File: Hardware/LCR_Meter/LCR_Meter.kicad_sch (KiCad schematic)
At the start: 0 parts

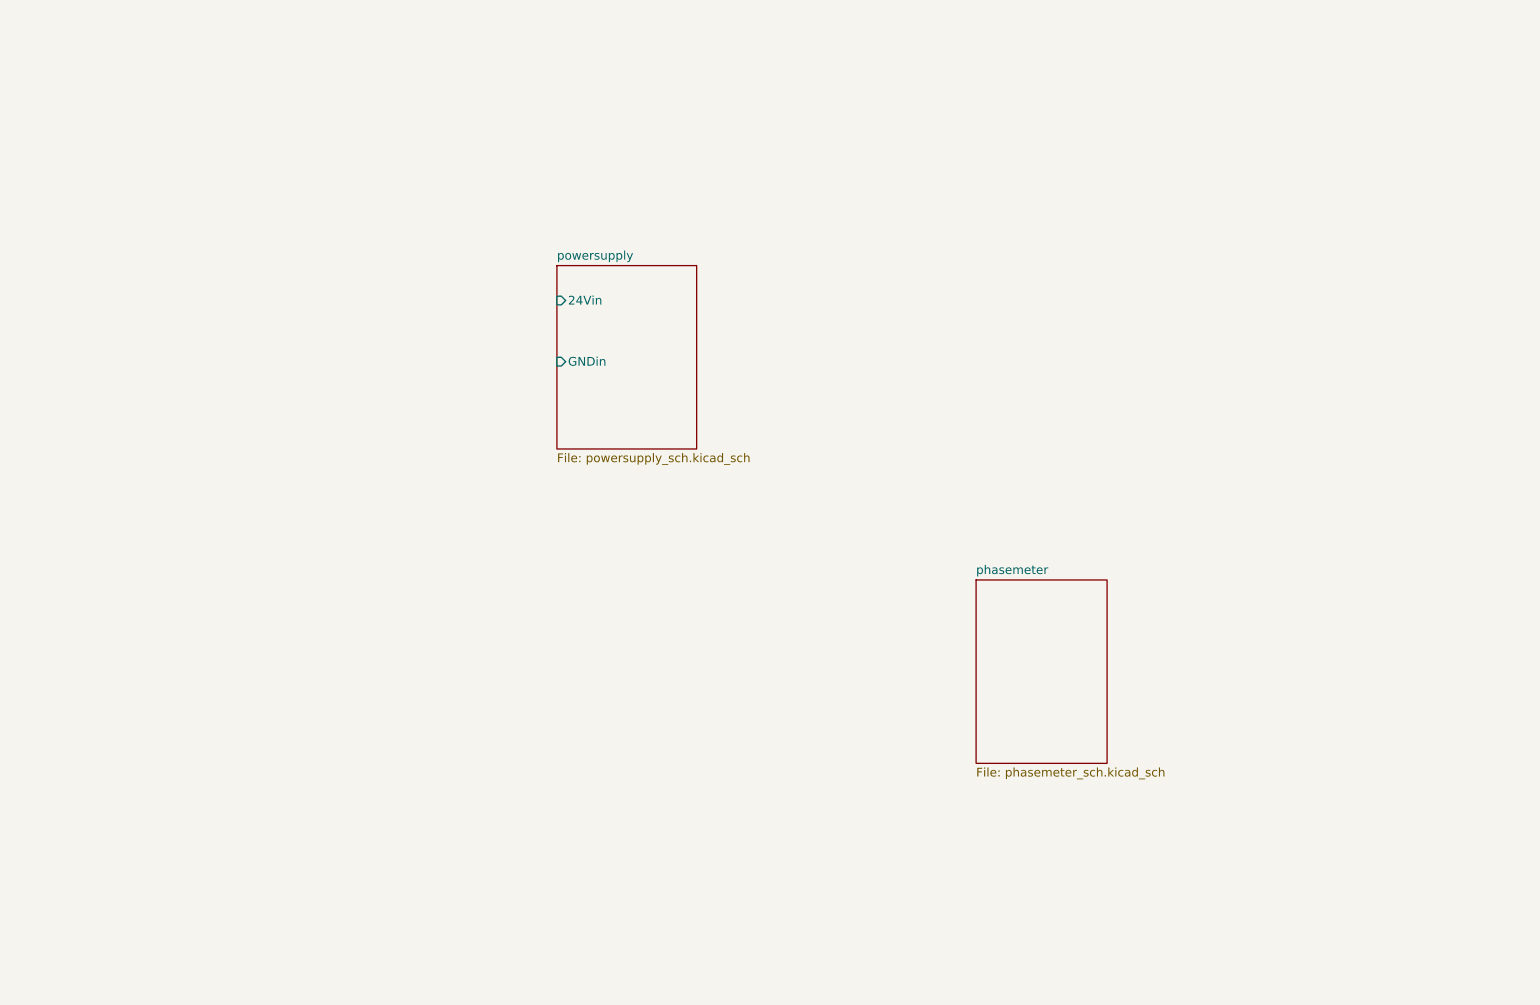
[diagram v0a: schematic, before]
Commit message: work on schematic block diagramm
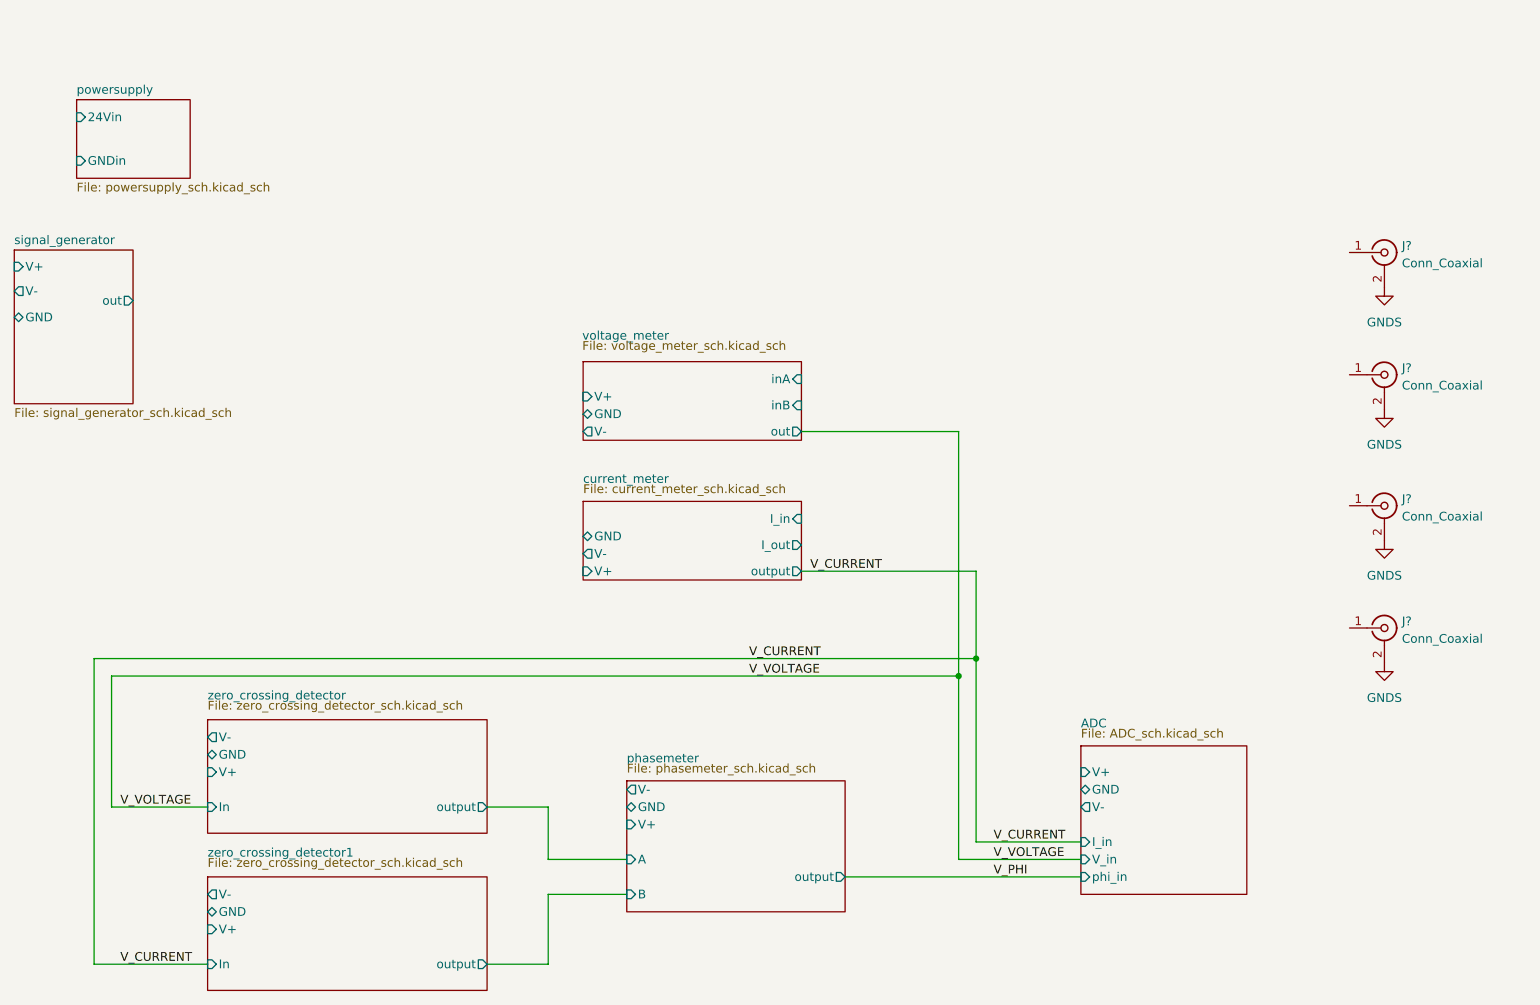
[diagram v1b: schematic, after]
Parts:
- added J? (x4): Conn_Coaxial, symbol Connector:Conn_Coaxial
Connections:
- new net GNDS: J?.2 (Ext), J?.2 (Ext), J?.2 (Ext), J?.2 (Ext)
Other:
- added sheet ADC (ADC_sch.kicad_sch)
- added sheet current_meter (current_meter_sch.kicad_sch)
- added sheet signal_generator (signal_generator_sch.kicad_sch)
- added sheet voltage_meter (voltage_meter_sch.kicad_sch)
- added sheet zero_crossing_detector (zero_crossing_detector_sch.kicad_sch)
- added sheet zero_crossing_detector1 (zero_crossing_detector_sch.kicad_sch)
- sheet phasemeter ports: added A, B, GND, V+, V-, output; removed none

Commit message: work on KCR schematic
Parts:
- J?: value Conn_Coaxial -> L_CUR; footprint (none) -> Connector_Coaxial:SMA_Amphenol_132291-12_Vertical
- J?: value Conn_Coaxial -> H_POT; footprint (none) -> Connector_Coaxial:SMA_Amphenol_132291-12_Vertical
- J?: value Conn_Coaxial -> L_POT; footprint (none) -> Connector_Coaxial:SMA_Amphenol_132291-12_Vertical
- J?: value Conn_Coaxial -> H_CUR; footprint (none) -> Connector_Coaxial:SMA_Amphenol_132291-12_Vertical
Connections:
- net L_CUR: now reaches J?.1 (In)
- net H_POT: now reaches J?.1 (In)
- net L_POT: now reaches J?.1 (In)
- net H_CUR: now reaches J?.1 (In)
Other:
- sheet phasemeter renamed zerocrossing_phase_detector
- removed sheet zero_crossing_detector
- removed sheet zero_crossing_detector1
- added sheet activ_rectifiers (activ_rectifiers_sch.kicad_sch)
- sheet current_meter ports: added none; removed I_out
- sheet zerocrossing_phase_detector: file phasemeter_sch.kicad_sch -> zerocrossing_phase_detector_sch.kicad_sch
- moved on the sheet: J?

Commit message: work on Phase detector
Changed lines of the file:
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@@
       (effects (font (size 1.27 1.27)) (justify right))
-    )
-    (pin "V-" output (at 120.65 127 180)
-      (effects (font (size 1.27 1.27)) (justify left))
     )
     (pin "GND" bidirectional (at 120.65 129.54 180)
@@
     )
     (pin "V+" input (at 120.65 132.08 180)
+      (effects (font (size 1.27 1.27)) (justify left))
+    )
+    (pin "V-" input (at 120.65 127 180)
       (effects (font (size 1.27 1.27)) (justify left))
     )
@@
       (reference "#PWR0104") (unit 1) (value "GNDS") (footprint "")
     )
+    (path "/d1422d36-ee99-4795-804f-b865553c7f13/08a9b504-957a-452e-9508-e5b0b1205a5d"
+      (reference "C?") (unit 1) (value "100n") (footprint "Capacitor_SMD:C_0805_2012Metric_Pad1.18x1.45mm_HandSolder")
+    )
     (path "/3366fbd2-b7c6-4ccb-afdd-03c00c73e9fc/098ad0ae-aeb1-42c0-bb17-5236427ef036"
       (reference "C?") (unit 1) (value "100n") (footprint "Capacitor_SMD:C_1206_3216Metric")
     )
+    (path "/d1422d36-ee99-4795-804f-b865553c7f13/0bd4f34c-719a-4a2f-9253-4be87b4fffea"
+      (reference "C?") (unit 1) (value "100n") (footprint "Capacitor_SMD:C_0805_2012Metric_Pad1.18x1.45mm_HandSolder")
+    )
     (path "/3366fbd2-b7c6-4ccb-afdd-03c00c73e9fc/3840940d-b0c9-4ab7-8bfa-8ee653f9a3e6"
       (reference "C?") (unit 1) (value "100n") (footprint "Capacitor_SMD:C_1206_3216Metric")
     )
+    (path "/d1422d36-ee99-4795-804f-b865553c7f13/ba98c343-27f7-433c-a31e-e5c72a4732e8"
+      (reference "C?") (unit 1) (value "100n") (footprint "Capacitor_SMD:C_0805_2012Metric_Pad1.18x1.45mm_HandSolder")
+    )
+    (path "/d1422d36-ee99-4795-804f-b865553c7f13/c7cb2033-4bc4-4f5b-9f35-08da814285af"
+      (reference "C?") (unit 1) (value "100n") (footprint "Capacitor_SMD:C_0805_2012Metric_Pad1.18x1.45mm_HandSolder")
+    )
     (path "/3366fbd2-b7c6-4ccb-afdd-03c00c73e9fc/0b3f0e18-090c-4545-bbd0-c5e5f41d899e"
       (reference "D?") (unit 1) (value "MMBD301LT3G") (footprint "Package_TO_SOT_SMD:SOT-23")
@@
       (reference "R?") (unit 1) (value "10k") (footprint "Resistor_SMD:R_1206_3216Metric")
     )
+    (path "/d1422d36-ee99-4795-804f-b865553c7f13/1e134a5a-6aee-4d56-b2fe-8ed1f3d172a0"
+      (reference "R?") (unit 1) (value "0R") (footprint "Resistor_SMD:R_1206_3216Metric")
+    )
     (path "/3366fbd2-b7c6-4ccb-afdd-03c00c73e9fc/444898c1-67a0-42b3-97be-98c41c93ac11"
       (reference "R?") (unit 1) (value "510") (footprint "Resistor_SMD:R_1206_3216Metric")
@@
       (reference "R?") (unit 1) (value "10k") (footprint "Resistor_SMD:R_1206_3216Metric")
     )
+    (path "/d1422d36-ee99-4795-804f-b865553c7f13/62801aac-92ca-4eae-8c61-979478e0e9ae"
+      (reference "R?") (unit 1) (value "0R") (footprint "Resistor_SMD:R_1206_3216Metric")
+    )
     (path "/3366fbd2-b7c6-4ccb-afdd-03c00c73e9fc/680f26b3-1b85-467d-bbc7-3845c6068a65"
       (reference "R?") (unit 1) (value "510") (footprint "Resistor_SMD:R_1206_3216Metric")
@@
       (reference "R?") (unit 1) (value "100") (footprint "Resistor_SMD:R_1206_3216Metric")
     )
+    (path "/d1422d36-ee99-4795-804f-b865553c7f13/e081acbc-dcd5-46f0-b16c-995c8afde600"
+      (reference "R?") (unit 1) (value "10k") (footprint "Resistor_SMD:R_1206_3216Metric")
+    )
+    (path "/d1422d36-ee99-4795-804f-b865553c7f13/e185ccfb-82b2-4fe5-862f-436648a7e1e6"
+      (reference "R?") (unit 1) (value "10k") (footprint "Resistor_SMD:R_1206_3216Metric")
+    )
+    (path "/d1422d36-ee99-4795-804f-b865553c7f13/2a1409ee-1293-4441-a87e-76d264eda319"
+      (reference "U?") (unit 1) (value "74HC74") (footprint "")
+    )
     (path "/f87a49d0-867e-497b-803c-a690fbe0238a/2a7bc947-2f91-4361-bf78-67ecee38e106"
       (reference "U?") (unit 1) (value "AD620") (footprint "")
     )
+    (path "/d1422d36-ee99-4795-804f-b865553c7f13/2f38035e-fe39-4c58-a766-bf27a6f67d29"
+      (reference "U?") (unit 1) (value "AD822ARZ") (footprint "Package_SO:SOIC-8_3.9x4.9mm_P1.27mm")
+    )
+    (path "/d1422d36-ee99-4795-804f-b865553c7f13/38c70d62-03ad-434a-af33-09684202360b"
+      (reference "U?") (unit 1) (value "74HC86") (footprint "")
+    )
     (path "/e2f440a9-67d9-4224-8882-d211dd4eecd4/3f05f0a1-36b6-400e-9ce2-5f3de2b2a52d"
       (reference "U?") (unit 1) (value "AD620") (footprint "")
@@
       (reference "U?") (unit 1) (value "LT1396CMS8") (footprint "Package_SO:MSOP-8_3x3mm_P0.65mm")
     )
+    (path "/d1422d36-ee99-4795-804f-b865553c7f13/537406b7-bbba-456a-9460-84309e6f6d3e"
+      (reference "U?") (unit 1) (value "ADA4860-1") (footprint "Package_TO_SOT_SMD:SOT-23-6")
+    )
+    (path "/d1422d36-ee99-4795-804f-b865553c7f13/7d72a520-ebd2-4153-895a-2e9e8dc7c80d"
+      (reference "U?") (unit 1) (value "74HC74") (footprint "")
+    )
     (path "/f87a49d0-867e-497b-803c-a690fbe0238a/86315ce1-6b22-4a95-a1df-beceed577bf4"
       (reference "U?") (unit 1) (value "AD8610") (footprint "")
@@
       (reference "U?") (unit 1) (value "AD8610") (footprint "")
     )
+    (path "/d1422d36-ee99-4795-804f-b865553c7f13/ef7b66bf-27ef-4f3a-b6ea-10fa66aa73b8"
+      (reference "U?") (unit 1) (value "ADA4860-1") (footprint "Package_TO_SOT_SMD:SOT-23-6")
+    )
+    (path "/d1422d36-ee99-4795-804f-b865553c7f13/0f341362-5e83-42f5-93be-12fa06a601f0"
+      (reference "U?") (unit 2) (value "74HC86") (footprint "")
+    )
     (path "/3366fbd2-b7c6-4ccb-afdd-03c00c73e9fc/93d12501-bd9b-43e0-8a54-ebbcb564b372"
       (reference "U?") (unit 2) (value "LT1396CMS8") (footprint "Package_SO:MSOP-8_3x3mm_P0.65mm")
     )
-  )
+    (path "/d1422d36-ee99-4795-804f-b865553c7f13/b969815b-8224-4c74-b1d9-d9373302641f"
+      (reference "U?") (unit 2) (value "74HC74") (footprint "")
+    )
+    (path "/d1422d36-ee99-4795-804f-b865553c7f13/ebbbeb47-2e32-4ad7-868f-f8c1a55c430b"
+      (reference "U?") (unit 2) (value "AD822ARZ") (footprint "Package_SO:SOIC-8_3.9x4.9mm_P1.27mm")
+    )
+    (path "/d1422d36-ee99-4795-804f-b865553c7f13/efce3918-34c9-4b85-8730-243fb88372c8"
+      (reference "U?") (unit 2) (value "74HC74") (footprint "")
+    )
+    (path "/d1422d36-ee99-4795-804f-b865553c7f13/066ad29d-d832-4754-8fdd-7be3e7c4cb3f"
+      (reference "U?") (unit 3) (value "74HC74") (footprint "")
+    )
+    (path "/d1422d36-ee99-4795-804f-b865553c7f13/e491fd52-a6ee-4f06-ba89-b7a0d0bf1c21"
+      (reference "U?") (unit 3) (value "74HC74") (footprint "")
+    )
+    (path "/d1422d36-ee99-4795-804f-b865553c7f13/fd1193a8-9977-4066-942d-114a9622c266"
+      (reference "U?") (unit 3) (value "74HC86") (footprint "")
+    )
+    (path "/d1422d36-ee99-4795-804f-b865553c7f13/0959ef5d-87fe-44da-8f3a-4f8a14dbe325"
+      (reference "U?") (unit 4) (value "74HC86") (footprint "")
+    )
+    (path "/d1422d36-ee99-4795-804f-b865553c7f13/8ecb312a-87ba-4459-bbdc-a724c31ed57b"
+      (reference "U?") (unit 5) (value "74HC86") (footprint "")
+    )
+  )

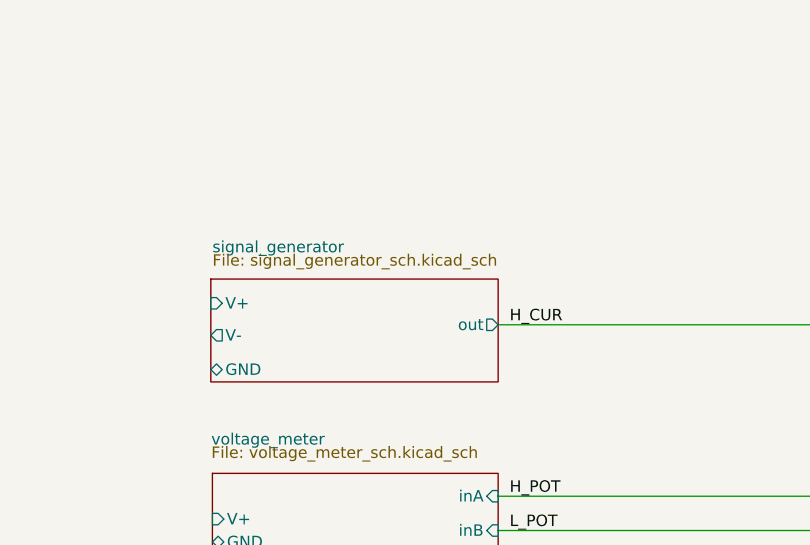
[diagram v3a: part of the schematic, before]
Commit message: work on signal generator
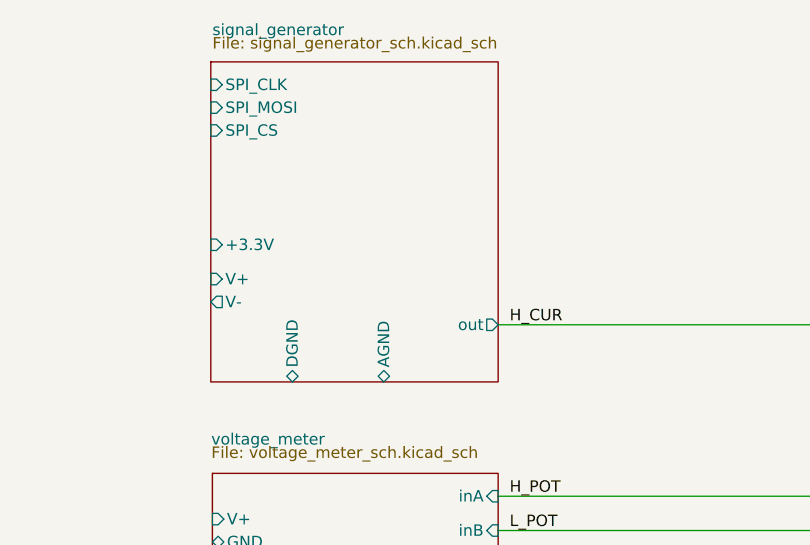
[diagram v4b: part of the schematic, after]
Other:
- sheet signal_generator ports: added +3.3V, AGND, DGND, SPI_CLK, SPI_CS, SPI_MOSI; removed GND
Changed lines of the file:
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@@
     )
   )
-  (sheet (at 120.4722 43.18) (size 31.9278 11.43)
+  (sheet (at 120.4722 19.05) (size 31.9278 35.56)
     (stroke (width 0.1524) (type solid) (color 0 0 0 0))
     (fill (color 0 0 0 0.0000))
-    (property "Sheet name" "signal_generator" (id 0) (at 120.65 40.3606 0)
+    (property "Sheet name" "signal_generator" (id 0) (at 120.65 16.2306 0)
       (effects (font (size 1.27 1.27)) (justify left bottom))
     )
-    (property "Sheet file" "signal_generator_sch.kicad_sch" (id 1) (at 120.65 40.3606 0)
+    (property "Sheet file" "signal_generator_sch.kicad_sch" (id 1) (at 120.65 16.2306 0)
       (effects (font (size 1.27 1.27)) (justify left top))
     )
-    (pin "V+" input (at 120.4722 45.8724 180)
-      (effects (font (size 1.27 1.27)) (justify left))
-    )
-    (pin "V-" output (at 120.4722 49.4284 180)
-      (effects (font (size 1.27 1.27)) (justify left))
-    )
-    (pin "GND" bidirectional (at 120.4722 53.2384 180)
+    (pin "V+" input (at 120.4722 43.18 180)
+      (effects (font (size 1.27 1.27)) (justify left))
+    )
+    (pin "V-" output (at 120.4722 45.72 180)
       (effects (font (size 1.27 1.27)) (justify left))
     )
     (pin "out" output (at 152.4 48.26 0)
       (effects (font (size 1.27 1.27)) (justify right))
+    )
+    (pin "DGND" bidirectional (at 129.54 54.61 270)
+      (effects (font (size 1.27 1.27)) (justify left))
+    )
+    (pin "AGND" bidirectional (at 139.7 54.61 270)
+      (effects (font (size 1.27 1.27)) (justify left))
+    )
+    (pin "SPI_CLK" input (at 120.4722 21.59 180)
+      (effects (font (size 1.27 1.27)) (justify left))
+    )
+    (pin "+3.3V" input (at 120.4722 39.37 180)
+      (effects (font (size 1.27 1.27)) (justify left))
+    )
+    (pin "SPI_MOSI" input (at 120.4722 24.13 180)
+      (effects (font (size 1.27 1.27)) (justify left))
+    )
+    (pin "SPI_CS" input (at 120.4722 26.67 180)
+      (effects (font (size 1.27 1.27)) (justify left))
     )
   )
@@
       (reference "C?") (unit 1) (value "100n") (footprint "Capacitor_SMD:C_0805_2012Metric_Pad1.18x1.45mm_HandSolder")
     )
+    (path "/eb72df69-0d7b-45d1-ac9b-f5f7558dee68/2bdb22ea-2bab-48ed-b8ca-f63d94caa458"
+      (reference "C?") (unit 1) (value "100n") (footprint "Capacitor_SMD:C_0805_2012Metric_Pad1.18x1.45mm_HandSolder")
+    )
     (path "/3366fbd2-b7c6-4ccb-afdd-03c00c73e9fc/3840940d-b0c9-4ab7-8bfa-8ee653f9a3e6"
       (reference "C?") (unit 1) (value "100n") (footprint "Capacitor_SMD:C_1206_3216Metric")
     )
+    (path "/eb72df69-0d7b-45d1-ac9b-f5f7558dee68/b91db108-d500-4f4b-954e-ee2212d0eea6"
+      (reference "C?") (unit 1) (value "10n") (footprint "Capacitor_SMD:C_0805_2012Metric_Pad1.18x1.45mm_HandSolder")
+    )
     (path "/d1422d36-ee99-4795-804f-b865553c7f13/ba98c343-27f7-433c-a31e-e5c72a4732e8"
       (reference "C?") (unit 1) (value "100n") (footprint "Capacitor_SMD:C_0805_2012Metric_Pad1.18x1.45mm_HandSolder")
     )
     (path "/d1422d36-ee99-4795-804f-b865553c7f13/c7cb2033-4bc4-4f5b-9f35-08da814285af"
+      (reference "C?") (unit 1) (value "100n") (footprint "Capacitor_SMD:C_0805_2012Metric_Pad1.18x1.45mm_HandSolder")
+    )
+    (path "/eb72df69-0d7b-45d1-ac9b-f5f7558dee68/df7dd165-5ad5-48b5-988d-c6c9838b4a66"
+      (reference "C?") (unit 1) (value "10n") (footprint "Capacitor_SMD:C_0805_2012Metric_Pad1.18x1.45mm_HandSolder")
+    )
+    (path "/eb72df69-0d7b-45d1-ac9b-f5f7558dee68/fa6ed327-7524-468a-8671-9fbb7cb3ac69"
       (reference "C?") (unit 1) (value "100n") (footprint "Capacitor_SMD:C_0805_2012Metric_Pad1.18x1.45mm_HandSolder")
     )
@@
       (reference "R?") (unit 1) (value "10k") (footprint "Resistor_SMD:R_1206_3216Metric")
     )
+    (path "/eb72df69-0d7b-45d1-ac9b-f5f7558dee68/eb26807c-3046-4abc-804b-c9ca56096a90"
+      (reference "R?") (unit 1) (value "1k") (footprint "Resistor_SMD:R_1206_3216Metric")
+    )
+    (path "/eb72df69-0d7b-45d1-ac9b-f5f7558dee68/1e679181-d56a-4634-9531-2980a7e124b5"
+      (reference "U?") (unit 1) (value "AD9833xRM") (footprint "Package_SO:MSOP-10_3x3mm_P0.5mm")
+    )
     (path "/d1422d36-ee99-4795-804f-b865553c7f13/2a1409ee-1293-4441-a87e-76d264eda319"
       (reference "U?") (unit 1) (value "74HC74") (footprint "")
@@
       (reference "U?") (unit 5) (value "74HC86") (footprint "")
     )
-  )
+    (path "/eb72df69-0d7b-45d1-ac9b-f5f7558dee68/91dc23dc-aadb-4461-94d4-43e68ae93f1f"
+      (reference "X?") (unit 1) (value "ASE-25.000MHZ") (footprint "Oscillator:Oscillator_SMD_Abracon_ASE-4Pin_3.2x2.5mm")
+    )
+  )
